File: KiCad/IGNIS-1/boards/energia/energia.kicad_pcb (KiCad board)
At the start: 2 copper layers, 62 x 62 mm, 8 parts, among them J40 Backplane, U3 Boost_5V

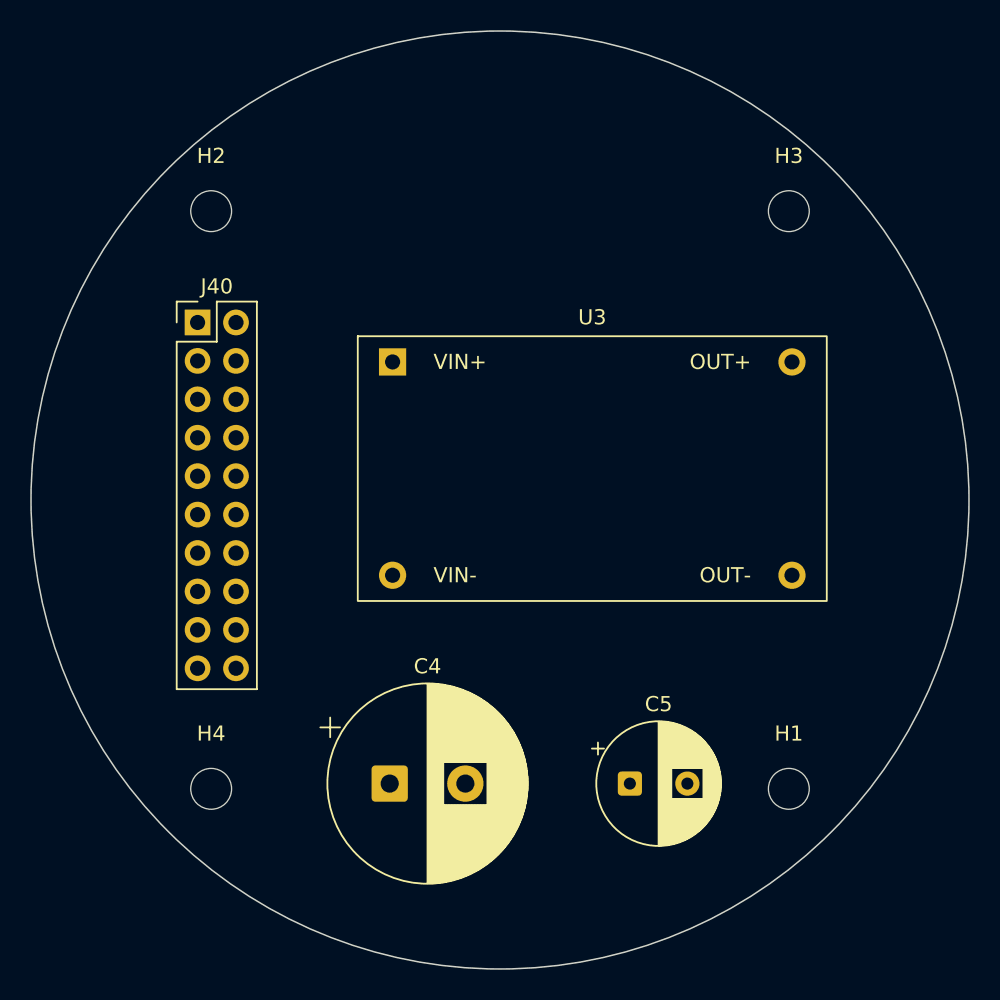
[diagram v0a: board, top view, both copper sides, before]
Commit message: wip: recableo backplane split en progreso (GUI) + doc con move TPS63020
Co-Authored-By: Claude Opus 4.8 <noreply@anthropic.com>
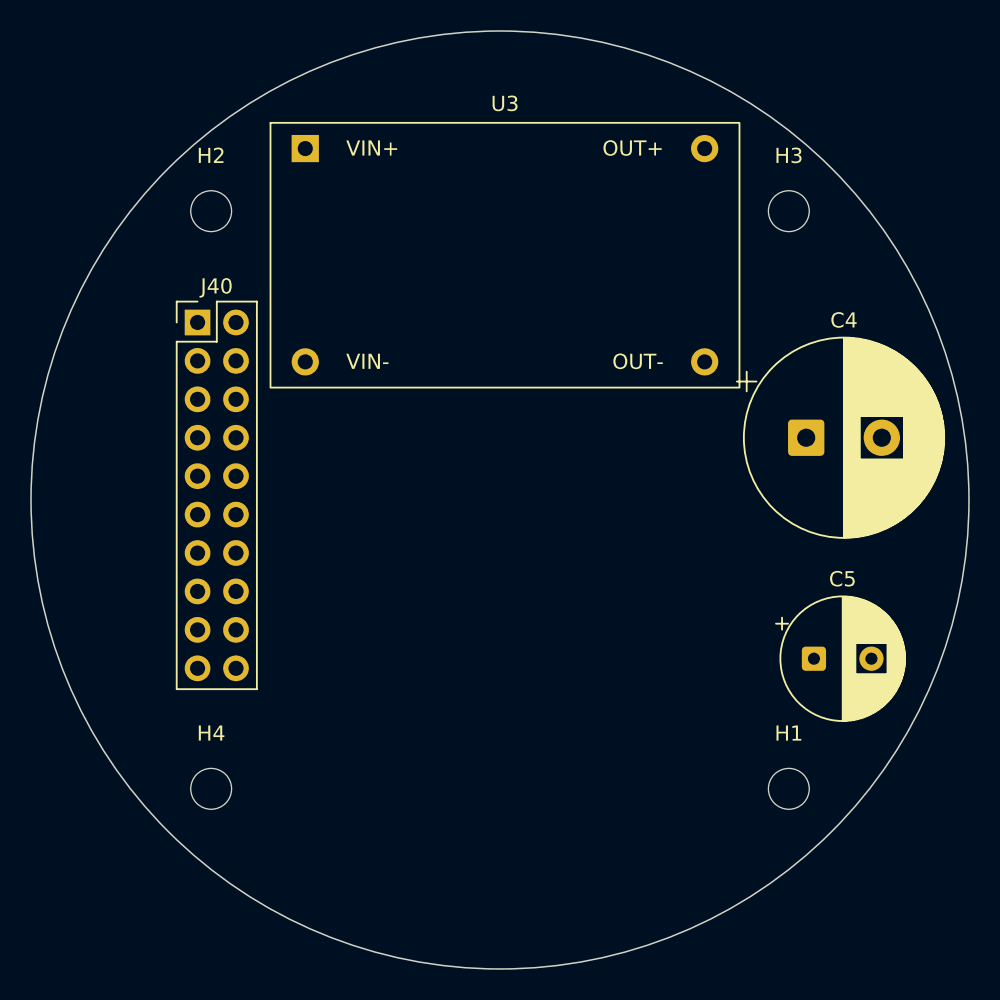
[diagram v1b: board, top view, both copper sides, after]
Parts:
- moved C4 35.8 mm to (120.2, 95.9)
- moved U3 15.2 mm to (100.3, 83.8)
- moved C5 14.7 mm to (120.8, 110.5)
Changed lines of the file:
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@@
 	(footprint "IGNIS1:MT3608_module"
 		(layer "F.Cu")
-		(at 106.1 97.925)
+		(at 100.33 83.82)
 		(descr "MT3608 adjustable boost module (HW-183B) - 31x17.5mm - 4 THT posts 26.4x14.1mm. Module mounts face-up, pins down (mezzanine). Top view 1:1, no mirror. Pad1=VIN+ TL, 2=VIN- BL, 3=OUT+ TR, 4=OUT- BR.")
 		(property "Reference" "U3"
@@
 	(footprint "Capacitor_THT:CP_Radial_D8.0mm_P3.80mm"
 		(layer "F.Cu")
-		(at 108.585 118.745)
+		(at 120.752349 110.49)
 		(descr "CP, Radial series, Radial, pin pitch=3.80mm, diameter=8mm, height=14mm, Electrolytic Capacitor")
 		(tags "CP Radial series Radial pin pitch 3.80mm diameter 8mm height 14mm Electrolytic Capacitor")
@@
 	(footprint "Capacitor_THT:CP_Radial_D13.0mm_P5.00mm"
 		(layer "F.Cu")
-		(at 92.71 118.745)
+		(at 120.239785 95.885)
 		(descr "CP, Radial series, Radial, pin pitch=5.00mm, diameter=13mm, height=20mm, Electrolytic Capacitor")
 		(tags "CP Radial series Radial pin pitch 5.00mm diameter 13mm height 20mm Electrolytic Capacitor")
